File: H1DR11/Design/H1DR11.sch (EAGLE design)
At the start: 34 parts, among them P1 HEXABIT_17.32_NO_P6, P2 RS-485, U1 STM32F091CBU6, U2 MAX14840EASAT, X1 XTALL_CSTCE8M00G52

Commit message: chnage connecter to pinheader
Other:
- note added: "VDD=3v3"
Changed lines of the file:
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@@
 <?xml version="1.0" encoding="utf-8"?>
 <!DOCTYPE eagle SYSTEM "eagle.dtd">
-<eagle version="9.5.1">
+<eagle version="9.6.0">
 <drawing>
 <settings>
@@
 <setting verticaltext="up"/>
 </settings>
-<grid distance="50" unitdist="mil" unit="mil" style="lines" multiple="1" display="yes" altdistance="0.01" altunitdist="inch" altunit="inch"/>
+<grid distance="0.1" unitdist="inch" unit="inch" style="lines" multiple="1" display="no" altdistance="0.01" altunitdist="inch" altunit="inch"/>
 <layers>
 <layer number="1" name="Top" color="4" fill="1" visible="no" active="no"/>
@@
 <text x="242.6462" y="6.1722" size="1.9304" layer="100" font="vector">www.hexabitz.com</text>
 <text x="195.7578" y="6.1214" size="1.9304" layer="101" font="vector" align="center">Amir Tabbakh</text>
+<text x="22.86" y="193.04" size="3.81" layer="94">VDD=3v3</text>
 </plain>
 <instances>
@@
 <text x="194.4878" y="11.2014" size="1.9304" layer="101" font="vector" align="center">RS485 Serial Transceiver</text>
 <text x="194.4878" y="6.1214" size="1.9304" layer="101" font="vector" align="center">Amir Tabbakh</text>
+<text x="35.56" y="187.96" size="3.81" layer="94">VDD=3v3</text>
 </plain>
 <instances>

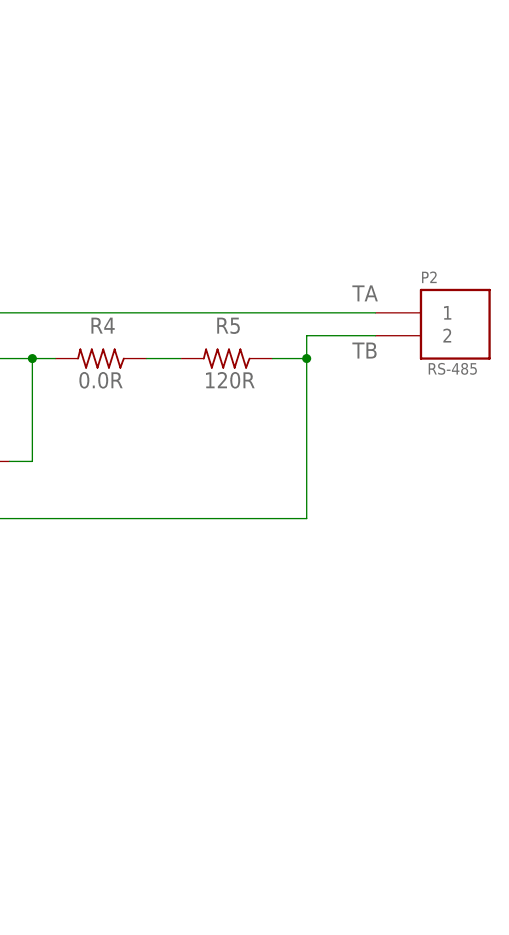
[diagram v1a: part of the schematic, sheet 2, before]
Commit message: fix  connector problems
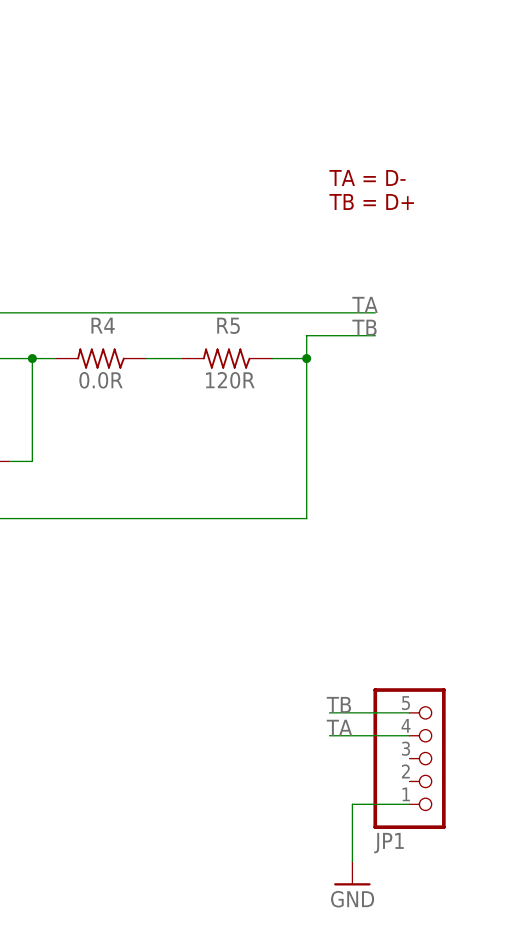
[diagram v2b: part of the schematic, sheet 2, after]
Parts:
- removed P2: RS-485, Hexabitz:1546111-2
- added JP1: (no value), Hexabitz:PINHD-1X5/90
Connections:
- net GND: now also JP1.1
- net TA: now also JP1.4; no longer P2.1
- net TB: now also JP1.5; no longer P2.2
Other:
- note added: "TA = D- TB = D+"
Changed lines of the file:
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@@
 <setting verticaltext="up"/>
 </settings>
-<grid distance="0.1" unitdist="inch" unit="inch" style="lines" multiple="1" display="no" altdistance="0.01" altunitdist="inch" altunit="inch"/>
+<grid distance="50" unitdist="mil" unit="mil" style="lines" multiple="1" display="yes" altdistance="0.01" altunitdist="inch" altunit="inch"/>
 <layers>
 <layer number="1" name="Top" color="4" fill="1" visible="no" active="no"/>
@@
 <part name="SUPPLY14" library="supply2" deviceset="VDD" device=""/>
 <part name="GND9" library="supply1" library_urn="urn:adsk.eagle:library:371" deviceset="GND" device=""/>
-<part name="P2" library="Hexabitz" deviceset="1546111-2" device="" value="RS-485"/>
 <part name="U2" library="Hexabitz" deviceset="MAX14840EASAT" device=""/>
 <part name="GND10" library="supply1" library_urn="urn:adsk.eagle:library:371" deviceset="GND" device=""/>
@@
 <attribute name="OCTOPART_URL" value="https://octopart.com/vlmy1300-gs08-vishay-21709204?r=sp"/>
 </part>
+<part name="GND16" library="supply1" library_urn="urn:adsk.eagle:library:371" deviceset="GND" device=""/>
+<part name="JP1" library="Hexabitz" deviceset="PINHD-1X5" device="/90" package3d_urn="urn:adsk.eagle:package:22467/2"/>
 </parts>
 <sheets>
@@
 <text x="194.4878" y="6.1214" size="1.9304" layer="101" font="vector" align="center">Amir Tabbakh</text>
 <text x="35.56" y="187.96" size="3.81" layer="94">VDD=3v3</text>
+<text x="232.41" y="130.81" size="1.778" layer="94">TA = D-
+TB = D+</text>
 </plain>
 <instances>
@@
 <attribute name="VALUE" x="36.83" y="101.6" size="1.778" layer="96"/>
 </instance>
-<instance part="P2" gate="G$1" x="247.65" y="116.84" smashed="yes" rot="MR0">
-<attribute name="NAME" x="244.475" y="122.682" size="1.27" layer="95" rot="MR0"/>
-<attribute name="VALUE" x="248.92" y="112.522" size="1.27" layer="96" rot="MR0"/>
-</instance>
 <instance part="U2" gate="A" x="137.16" y="114.3" smashed="yes">
 <attribute name="NAME" x="124.46" y="135.62" size="2.0828" layer="95" ratio="10" rot="SR0"/>
@@
 <attribute name="VALUE" x="204.47" y="110.998" size="1.778" layer="96"/>
 </instance>
+<instance part="GND16" gate="1" x="234.95" y="55.88" smashed="yes" rot="MR0">
+<attribute name="VALUE" x="237.49" y="53.34" size="1.778" layer="96" rot="MR0"/>
+</instance>
+<instance part="JP1" gate="A" x="243.84" y="69.85" smashed="yes" rot="MR180">
+<attribute name="NAME" x="237.49" y="61.595" size="1.778" layer="95" rot="MR180"/>
+<attribute name="VALUE" x="237.49" y="80.01" size="1.778" layer="96" rot="MR180"/>
+</instance>
 </instances>
 <busses>
@@
 <wire x1="111.76" y1="88.9" x2="111.76" y2="90.17" width="0.1524" layer="91"/>
 </segment>
+<segment>
+<wire x1="241.3" y1="64.77" x2="234.95" y2="64.77" width="0.1524" layer="91"/>
+<wire x1="234.95" y1="64.77" x2="234.95" y2="58.42" width="0.1524" layer="91"/>
+<pinref part="GND16" gate="1" pin="GND"/>
+<pinref part="JP1" gate="A" pin="1"/>
+</segment>
 </net>
 <net name="UART1_TX" class="0">
@@
 <wire x1="154.94" y1="114.3" x2="175.26" y2="114.3" width="0.1524" layer="91"/>
 <wire x1="175.26" y1="114.3" x2="175.26" y2="96.52" width="0.1524" layer="91"/>
-<pinref part="P2" gate="G$1" pin="2"/>
-<wire x1="237.49" y1="116.84" x2="229.87" y2="116.84" width="0.1524" layer="91"/>
 <wire x1="229.87" y1="116.84" x2="229.87" y2="114.3" width="0.1524" layer="91"/>
 <wire x1="229.87" y1="114.3" x2="229.87" y2="96.52" width="0.1524" layer="91"/>
@@
 <wire x1="226.06" y1="114.3" x2="229.87" y2="114.3" width="0.1524" layer="91"/>
 <junction x="229.87" y="114.3"/>
-<label x="234.95" y="114.3" size="1.778" layer="95"/>
+<label x="234.95" y="116.84" size="1.778" layer="95"/>
+<wire x1="237.49" y1="116.84" x2="229.87" y2="116.84" width="0.1524" layer="91"/>
+</segment>
+<segment>
+<wire x1="241.3" y1="74.93" x2="232.41" y2="74.93" width="0.1524" layer="91"/>
+<label x="234.95" y="74.93" size="1.778" layer="95" rot="MR0"/>
+<pinref part="JP1" gate="A" pin="5"/>
 </segment>
 </net>
@@
 <pinref part="U2" gate="A" pin="A"/>
 <wire x1="154.94" y1="119.38" x2="184.15" y2="119.38" width="0.1524" layer="91"/>
-<pinref part="P2" gate="G$1" pin="1"/>
 <pinref part="C12" gate="G$1" pin="1"/>
 <wire x1="184.15" y1="119.38" x2="237.49" y2="119.38" width="0.1524" layer="91"/>
@@
 <wire x1="184.15" y1="102.87" x2="186.69" y2="102.87" width="0.1524" layer="91"/>
 <junction x="184.15" y="114.3"/>
-<label x="234.95" y="120.65" size="1.778" layer="95"/>
+<label x="234.95" y="119.38" size="1.778" layer="95"/>
+</segment>
+<segment>
+<wire x1="241.3" y1="72.39" x2="232.41" y2="72.39" width="0.1524" layer="91"/>
+<label x="234.95" y="72.39" size="1.778" layer="95" rot="MR0"/>
+<pinref part="JP1" gate="A" pin="4"/>
 </segment>
 </net>
@@
 </drawing>
 <compatibility>
+<note version="6.3" minversion="6.2.2" severity="warning">
+Since Version 6.2.2 text objects can contain more than one line,
+which will not be processed correctly with this version.
+</note>
 <note version="8.2" severity="warning">
 Since Version 8.2, EAGLE supports online libraries. The ids
@@
 will not be understood (or retained) with this version.
 </note>
+<note version="8.3" severity="warning">
+Since Version 8.3, EAGLE supports the association of 3D packages
+with devices in libraries, schematics, and board files. Those 3D
+packages will not be understood (or retained) with this version.
+</note>
 </compatibility>
